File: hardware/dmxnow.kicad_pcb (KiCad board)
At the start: 2 copper layers, 146 x 65.5 mm, 76 parts, among them J1 WAGO 2604-1102 (L N in), J2 DMX tail (1 GND 2 B 3 A), J3 PROG (3V3 GND D- D+ EN BOOT 5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, J4 WAGO 2604-1102 (L_SW N out 1), J5 WAGO 2604-1102 (VLED_IN GND_L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, J6 WAGO 2604-1105 (VLED CH1-CH4), J7 WAGO 2604-1102 (L_SW N out 2,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, K1 G5RL-1A-E-HR DC5, Q1 AO3400A, Q2 AOD2610E, Q3 AOD2610E, Q4 AOD2610E, Q5 AOD2610E, SW1 PTS810 (BOOT/maintenance), U1 ESP32-C3-MINI-1-N4, U2 SP3485EN, U3 AP2112K-3.3, U4 74AHCT125

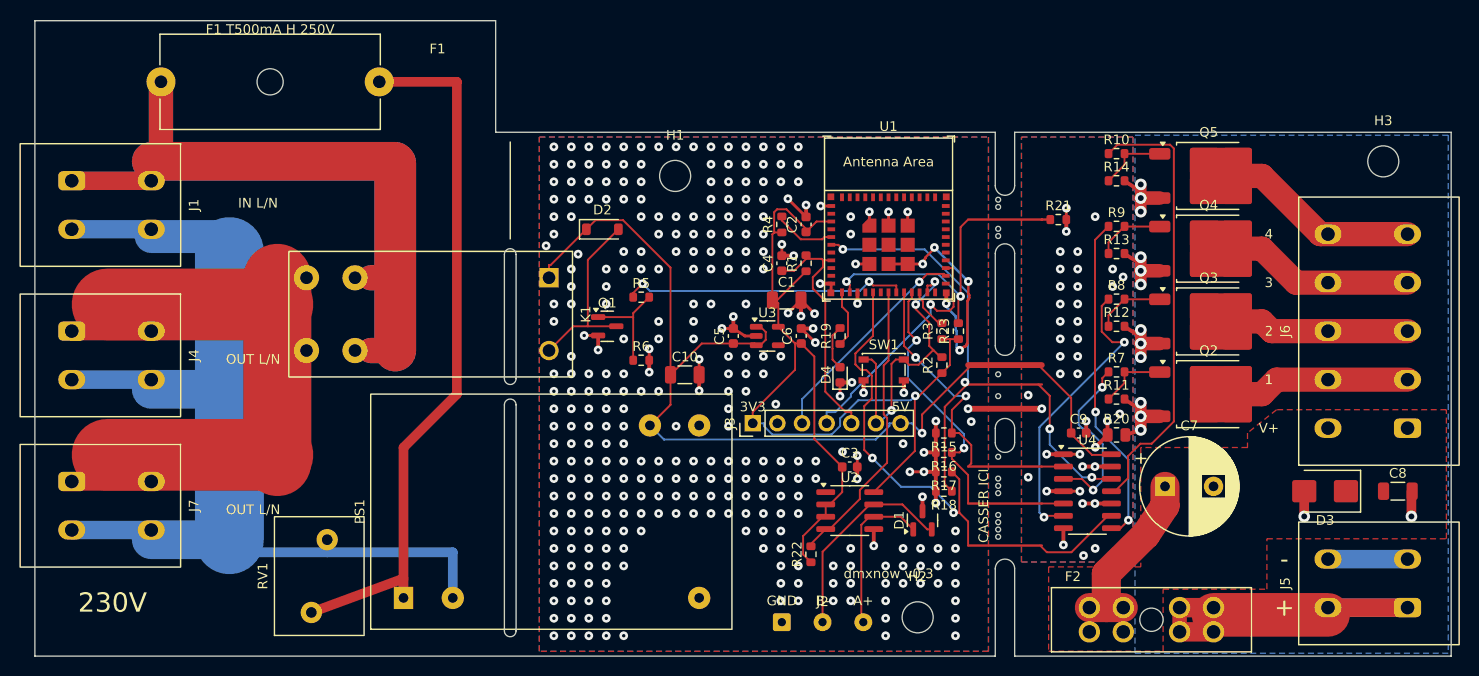
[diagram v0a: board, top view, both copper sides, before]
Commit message: hardware: J6 WAGO 2604-1105 (arrêté) remplacé par 2604-1102 + 2604-1103
Le 2604-1105 est « Discontinued » chez WAGO et à 0 chez JLCPCB. J6 devient
un 2604-1102 (VLED, CH1) et J8 un 2604-1103 (CH2-CH4), tous deux en stock et
de nouveau dans les fichiers d'assemblage JLCPCB.

- Blocs juxtaposés : 7,4 mm entre broches voisines d'après la fiche
  (L = (n - 1) x 5 + 7,4 mm) ; 8,0 mm au PCB (CH1 y 28,5 -> CH2 y 20,5).
  CH2-CH4 inchangés ; VLED et CH1 descendent de 3 mm.
- D3 passe à la verticale entre C7 et J6 ; C8 descend entre J6 et J5 ;
  plan VLED et pistes CH1 / GND_LED ajustés.
- SPEC, ADR 0008 (amendement), REVIEW, README : références, coût,
  remarque de commande.

Contrôles : netlist 0, PCB 0, DRC 0 erreur / 0 non connecté, canari OK.

Co-Authored-By: Claude Opus 5.5 <noreply@anthropic.com>
Claude-Session: https://claude.ai/code/session_01B51M6ZY5abLxTmcevvc8Le
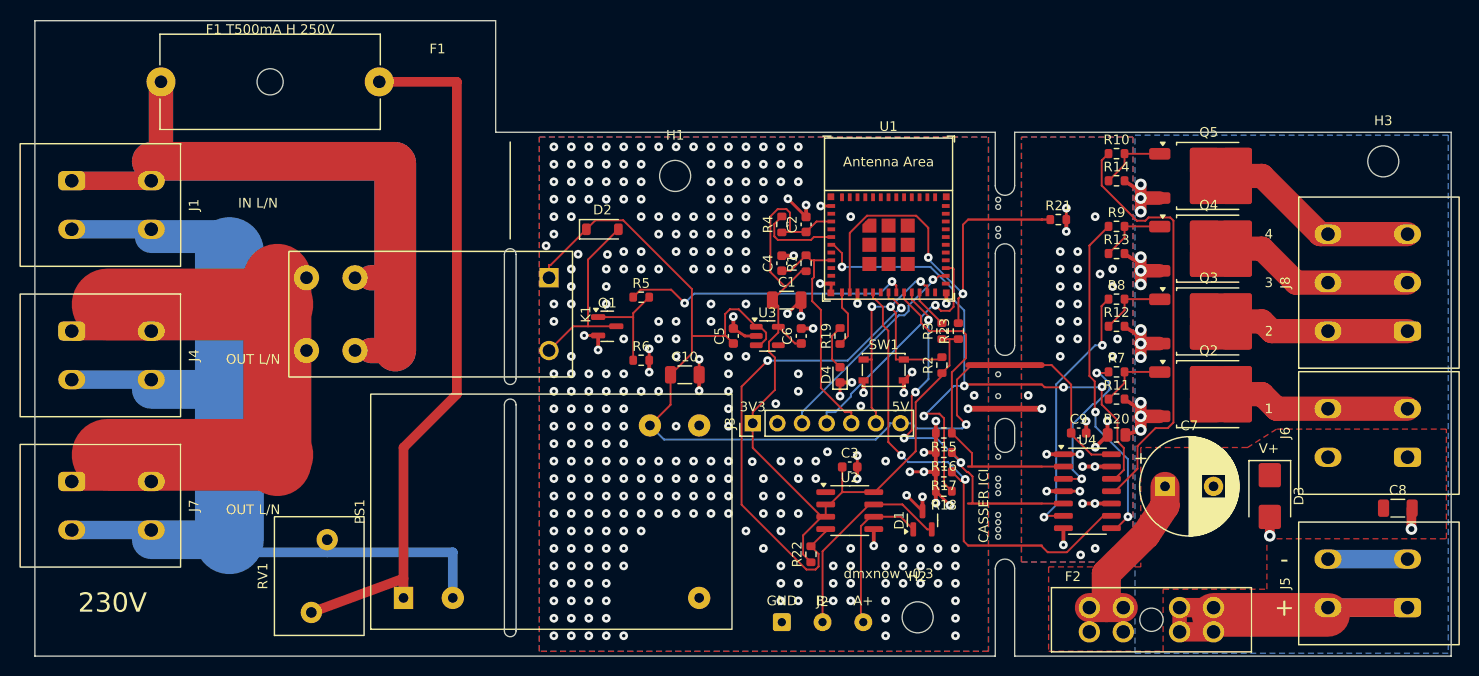
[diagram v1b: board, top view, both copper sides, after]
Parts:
- added J8: WAGO 2604-1103 (CH2-CH4), dmxnow:TerminalBlock_WAGO_2604-1103_1x03_P5.00mm_Horizontal, F.Cu at (191.5, 70.5)
- J6: value WAGO 2604-1105 (VLED CH1-CH4) -> WAGO 2604-1102 (VLED CH1); footprint dmxnow:TerminalBlock_WAGO_2604-1105_1x05_P5.00mm_Horizontal -> dmxnow:TerminalBlock_WAGO_2604-1102_1x02_P5.00mm_Horizontal
- moved D3 5.72 mm to (177.3, 87.5), turned to -90 degrees
- moved J6 3.00 mm to (191.5, 83.5)
- moved C8 1.75 mm to (190.5, 88.8)
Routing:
- net GND: track 120.3 -> 90.1 mm, vias 364 -> 337
- net DMX_TX: track 30.0 -> 50.1 mm, vias 0 -> 2
- net +3V3: track 105.4 -> 89.2 mm, vias 1 -> 0
- net BOARD_SENSE: track 33.8 -> 43.3 mm
- net PWM4: track 60.3 -> 67.0 mm, vias 4 -> 5
- net +5V: track 108.6 -> 114.1 mm
- net PWM3: track 56.1 -> 51.1 mm
- net PWM2: track 36.5 -> 39.8 mm, vias 2 -> 4
- net DRV2: track 30.3 -> 27.8 mm
- net IO2_PU: track 6.42 -> 8.53 mm
- net DRV4: track 46.2 -> 44.3 mm
- net DRV1: track 18.7 -> 16.9 mm
- net GND_LED: track 42.2 -> 41.1 mm
- net PWM1: track 33.1 -> 33.9 mm, vias 2 -> 0
- net USB_DM: track 22.7 -> 22.2 mm
